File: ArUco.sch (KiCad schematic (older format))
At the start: 1 part, among them J18 Conn_01x02

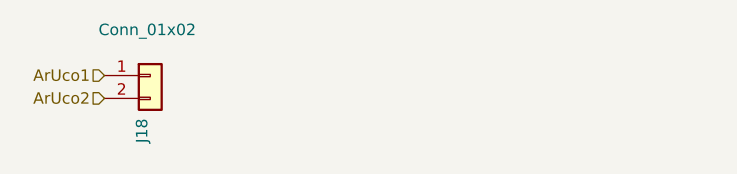
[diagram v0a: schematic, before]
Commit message: some more changes after Hugo's review, motors connectors not updated
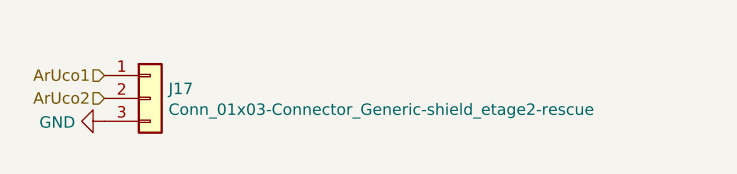
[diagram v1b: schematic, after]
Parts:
- removed J18: Conn_01x02, Connector_JST:JST_EH_B2B-EH-A_1x02_P2.50mm_Vertical, symbol shield_etage2-rescue:Conn_01x02-Connector_Generic-shield_etage2-rescue
- added J17: Conn_01x03-Connector_Generic-shield_etage2-rescue, Connector_JST:JST_EH_B3B-EH-A_1x03_P2.50mm_Vertical, symbol shield_etage2-rescue:Conn_01x03-Connector_Generic-shield_etage2-rescue
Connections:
- net ArUco1: now also J17.1 (Pin_1)
- net ArUco2: now also J17.2 (Pin_2)
- new net GND: J17.3 (Pin_3)
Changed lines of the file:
@@
 Comment4 ""
 $EndDescr
-$Comp
-L shield_etage2-rescue:Conn_01x02-Connector_Generic-shield_etage2-rescue J?
-U 1 1 5F826EBE
-P 6000 3100
-AR Path="/5F826EBE" Ref="J?"  Part="1"
-AR Path="/5F81CFC3/5F826EBE" Ref="J18"  Part="1"
-AR Path="/5F882FF7/5F826EBE" Ref="J?"  Part="1"
-F 0 "J18" V 5964 2912 50  0000 R CNN
-F 1 "Conn_01x02" H 6200 3300 50  0000 R CNN
-F 2 "Connector_JST:JST_EH_B2B-EH-A_1x02_P2.50mm_Vertical" H 6000 3100 50  0001 C CNN
-F 3 "~" H 6000 3100 50  0001 C CNN
-	1    6000 3100
-	1    0    0    -1
-$EndComp
 Text HLabel 5800 3100 0    50   Input ~ 0
 ArUco1
 Text HLabel 5800 3200 0    50   Input ~ 0
 ArUco2
+$Comp
+L power:GND #PWR0102
+U 1 1 5F889862
+P 5800 3300
+F 0 "#PWR0102" H 5800 3050 50  0001 C CNN
+F 1 "GND" V 5805 3172 50  0000 R CNN
+F 2 "" H 5800 3300 50  0001 C CNN
+F 3 "" H 5800 3300 50  0001 C CNN
+	1    5800 3300
+	0    1    1    0
+$EndComp
+$Comp
+L shield_etage2-rescue:Conn_01x03-Connector_Generic-shield_etage2-rescue J17
+U 1 1 5F88A6DF
+P 6000 3200
+F 0 "J17" H 6080 3242 50  0000 L CNN
+F 1 "Conn_01x03-Connector_Generic-shield_etage2-rescue" H 6080 3151 50  0000 L CNN
+F 2 "Connector_JST:JST_EH_B3B-EH-A_1x03_P2.50mm_Vertical" H 6000 3200 50  0001 C CNN
+F 3 "" H 6000 3200 50  0001 C CNN
+	1    6000 3200
+	1    0    0    -1
+$EndComp
 $EndSCHEMATC
